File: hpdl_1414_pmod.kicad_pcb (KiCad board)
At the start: 2 copper layers, 84 x 56 mm, 6 parts, among them J1 10129382-912001BLF, J2 10129382-912001BLF

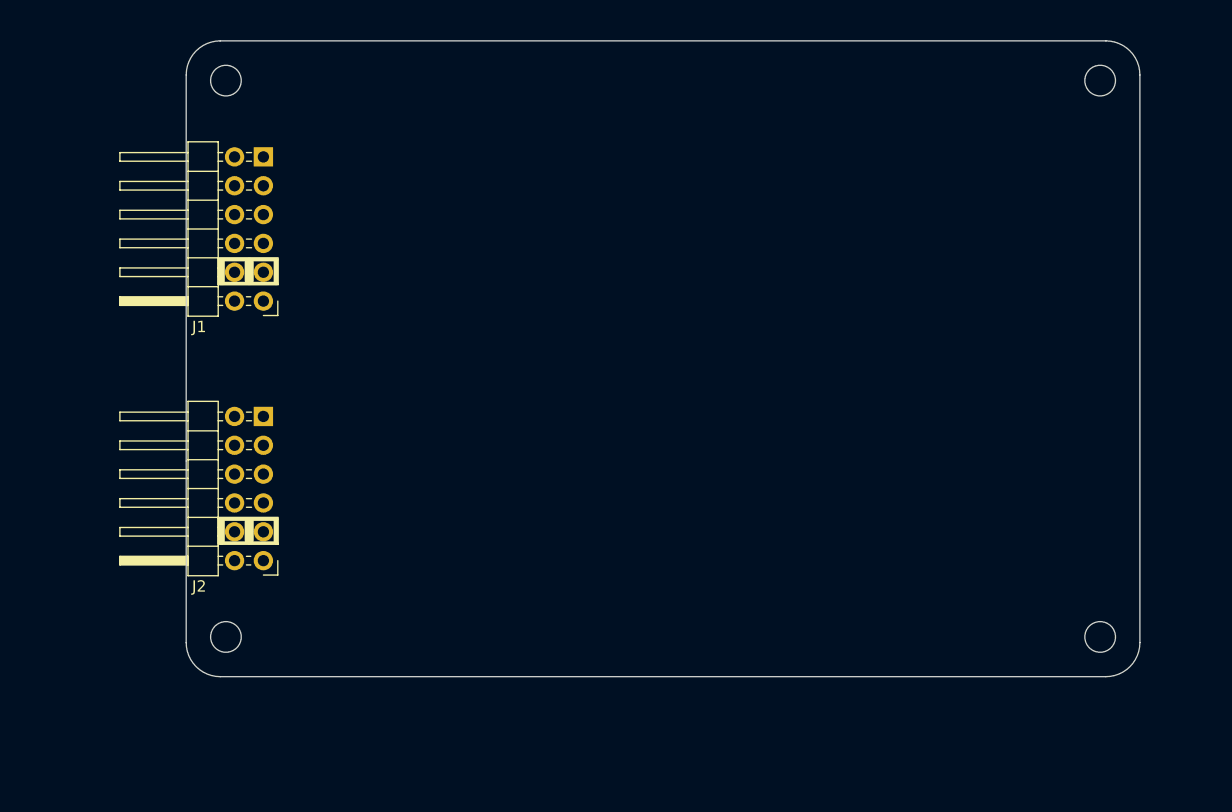
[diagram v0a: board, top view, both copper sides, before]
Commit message: Change pcb mounting hole type
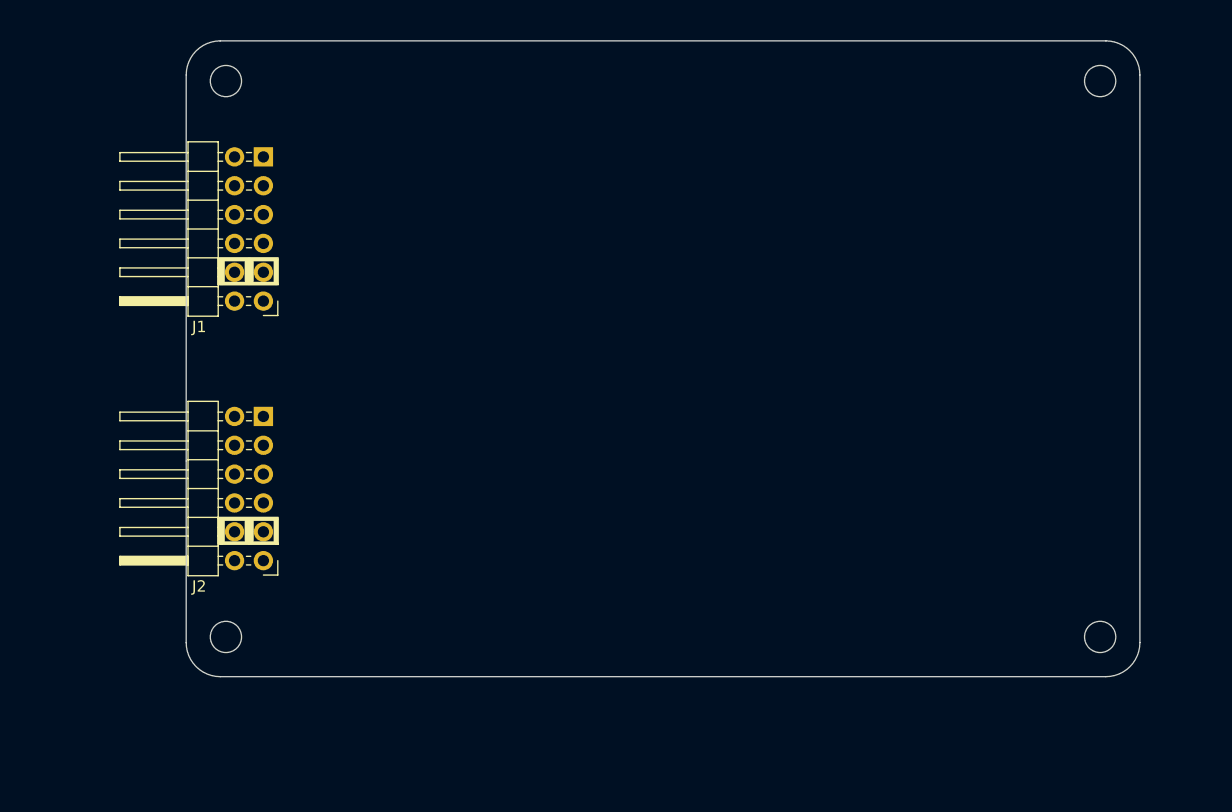
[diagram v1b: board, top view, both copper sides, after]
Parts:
- removed MH1, MH2, MH3, MH4: MountingHole_2.7mm_M2.5, MountingHole:MountingHole_2.7mm_M2.5
- added ?: , RPi_Hat:RPi_Hat_Mounting_Hole, F.Cu at (103.5, 96.5)
- added ?: , RPi_Hat:RPi_Hat_Mounting_Hole, F.Cu at (103.5, 47.5)
- added ?: , RPi_Hat:RPi_Hat_Mounting_Hole, F.Cu at (180.5, 47.5)
- added ?: , RPi_Hat:RPi_Hat_Mounting_Hole, F.Cu at (180.5, 96.5)
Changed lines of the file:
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@@
   (net 23 "unconnected-(J2-GND-Pad11)")
   (net 24 "unconnected-(J2-VCC-Pad12)")
-  (footprint "MountingHole:MountingHole_2.7mm_M2.5" locked (layer "F.Cu")
-    (at 180.5 47.5)
-    (descr "Mounting Hole 2.7mm, no annular, M2.5")
-    (tags "mounting hole 2.7mm no annular m2.5")
-    (attr board_only exclude_from_pos_files exclude_from_bom)
-    (fp_text reference "MH2" (at 0 4) (layer "F.Fab") hide
-        (effects (font (size 1 1) (thickness 0.15)))
-    )
-    (fp_text value "MountingHole_2.7mm_M2.5" (at 0 3.7) (layer "F.Fab") hide
-        (effects (font (size 1 1) (thickness 0.15)))
-    )
-    (fp_text user "${REFERENCE}" (at 0.3 0) (layer "F.Fab") hide
-        (effects (font (size 1 1) (thickness 0.15)))
-    )
-    (fp_circle (center 0 0) (end 2.7 0)
-      (stroke (width 0.15) (type solid)) (fill none) (layer "Cmts.User"))
-    (fp_circle (center 0 0) (end 2.95 0)
-      (stroke (width 0.05) (type solid)) (fill none) (layer "F.CrtYd"))
-    (pad "" np_thru_hole circle locked (at 0 0) (size 2.7 2.7) (drill 2.7) (layers "*.Cu" "*.Mask"))
-  )
-  (footprint "MountingHole:MountingHole_2.7mm_M2.5" locked (layer "F.Cu")
-    (at 103.5 96.5)
-    (descr "Mounting Hole 2.7mm, no annular, M2.5")
-    (tags "mounting hole 2.7mm no annular m2.5")
-    (attr board_only exclude_from_pos_files exclude_from_bom)
-    (fp_text reference "MH3" (at 0 -4) (layer "F.Fab") hide
-        (effects (font (size 1 1) (thickness 0.15)))
-    )
-    (fp_text value "MountingHole_2.7mm_M2.5" (at 0 3.7) (layer "F.Fab") hide
-        (effects (font (size 1 1) (thickness 0.15)))
-    )
-    (fp_text user "${REFERENCE}" (at 0.3 0) (layer "F.Fab") hide
-        (effects (font (size 1 1) (thickness 0.15)))
-    )
-    (fp_circle (center 0 0) (end 2.7 0)
-      (stroke (width 0.15) (type solid)) (fill none) (layer "Cmts.User"))
-    (fp_circle (center 0 0) (end 2.95 0)
-      (stroke (width 0.05) (type solid)) (fill none) (layer "F.CrtYd"))
-    (pad "" np_thru_hole circle locked (at 0 0) (size 2.7 2.7) (drill 2.7) (layers "*.Cu" "*.Mask"))
-  )
-  (footprint "MountingHole:MountingHole_2.7mm_M2.5" locked (layer "F.Cu")
-    (at 103.5 47.5)
-    (descr "Mounting Hole 2.7mm, no annular, M2.5")
-    (tags "mounting hole 2.7mm no annular m2.5")
-    (attr board_only exclude_from_pos_files exclude_from_bom)
-    (fp_text reference "MH1" (at 0 4) (layer "F.Fab") hide
-        (effects (font (size 1 1) (thickness 0.15)))
-    )
-    (fp_text value "MountingHole_2.7mm_M2.5" (at 0 3.7) (layer "F.Fab") hide
-        (effects (font (size 1 1) (thickness 0.15)))
-    )
-    (fp_text user "${REFERENCE}" (at 0.3 0) (layer "F.Fab") hide
-        (effects (font (size 1 1) (thickness 0.15)))
-    )
-    (fp_circle (center 0 0) (end 2.7 0)
-      (stroke (width 0.15) (type solid)) (fill none) (layer "Cmts.User"))
-    (fp_circle (center 0 0) (end 2.95 0)
-      (stroke (width 0.05) (type solid)) (fill none) (layer "F.CrtYd"))
-    (pad "" np_thru_hole circle locked (at 0 0) (size 2.7 2.7) (drill 2.7) (layers "*.Cu" "*.Mask"))
+  (footprint "RPi_Hat:RPi_Hat_Mounting_Hole" locked (layer "F.Cu")
+    (at 103.5 96.5 180)
+    (descr "Mounting hole, Befestigungsbohrung, 2,7mm, No Annular, Kein Restring,")
+    (tags "Mounting hole, Befestigungsbohrung, 2,7mm, No Annular, Kein Restring,")
+    (attr through_hole)
+    (fp_text reference "" (at 0 -4.0005 unlocked) (layer "F.SilkS") hide
+        (effects (font (size 1 1) (thickness 0.15)))
+    )
+    (fp_text value "" (at 0.09906 3.59918) (layer "F.Fab") hide
+        (effects (font (size 0.5 0.5) (thickness 0.07)))
+    )
+    (fp_circle (center 0 0) (end 3.1 0)
+      (stroke (width 0.15) (type solid)) (fill none) (layer "B.CrtYd"))
+    (fp_circle (center 0 0) (end 3.1 0)
+      (stroke (width 0.15) (type solid)) (fill none) (layer "F.CrtYd"))
+    (fp_circle (center 0 0) (end 1.375 0)
+      (stroke (width 0.15) (type solid)) (fill none) (layer "B.Fab"))
+    (fp_circle (center 0 0) (end 3.1 0)
+      (stroke (width 0.15) (type solid)) (fill none) (layer "B.Fab"))
+    (fp_circle (center 0 0) (end 1.375 0)
+      (stroke (width 0.15) (type solid)) (fill none) (layer "F.Fab"))
+    (fp_circle (center 0 0) (end 3.1 0)
+      (stroke (width 0.15) (type solid)) (fill none) (layer "F.Fab"))
+    (pad "" np_thru_hole circle locked (at 0 0 180) (size 2.75 2.75) (drill 2.75) (layers "F&B.Cu" "*.Mask")
+      (solder_mask_margin 1.725) (clearance 1.725))
+  )
+  (footprint "RPi_Hat:RPi_Hat_Mounting_Hole" locked (layer "F.Cu")
+    (at 103.5 47.54 180)
+    (descr "Mounting hole, Befestigungsbohrung, 2,7mm, No Annular, Kein Restring,")
+    (tags "Mounting hole, Befestigungsbohrung, 2,7mm, No Annular, Kein Restring,")
+    (attr through_hole)
+    (fp_text reference "" (at 0 -4.0005 unlocked) (layer "F.SilkS") hide
+        (effects (font (size 1 1) (thickness 0.15)))
+    )
+    (fp_text value "" (at 0.09906 3.59918) (layer "F.Fab") hide
+        (effects (font (size 0.5 0.5) (thickness 0.07)))
+    )
+    (fp_circle (center 0 0) (end 3.1 0)
+      (stroke (width 0.15) (type solid)) (fill none) (layer "B.CrtYd"))
+    (fp_circle (center 0 0) (end 3.1 0)
+      (stroke (width 0.15) (type solid)) (fill none) (layer "F.CrtYd"))
+    (fp_circle (center 0 0) (end 1.375 0)
+      (stroke (width 0.15) (type solid)) (fill none) (layer "B.Fab"))
+    (fp_circle (center 0 0) (end 3.1 0)
+      (stroke (width 0.15) (type solid)) (fill none) (layer "B.Fab"))
+    (fp_circle (center 0 0) (end 1.375 0)
+      (stroke (width 0.15) (type solid)) (fill none) (layer "F.Fab"))
+    (fp_circle (center 0 0) (end 3.1 0)
+      (stroke (width 0.15) (type solid)) (fill none) (layer "F.Fab"))
+    (pad "" np_thru_hole circle locked (at 0 0 180) (size 2.75 2.75) (drill 2.75) (layers "F&B.Cu" "*.Mask")
+      (solder_mask_margin 1.725) (clearance 1.725))
+  )
+  (footprint "RPi_Hat:RPi_Hat_Mounting_Hole" locked (layer "F.Cu")
+    (at 180.5 47.54 180)
+    (descr "Mounting hole, Befestigungsbohrung, 2,7mm, No Annular, Kein Restring,")
+    (tags "Mounting hole, Befestigungsbohrung, 2,7mm, No Annular, Kein Restring,")
+    (attr through_hole)
+    (fp_text reference "" (at 0 -4.0005 unlocked) (layer "F.SilkS") hide
+        (effects (font (size 1 1) (thickness 0.15)))
+    )
+    (fp_text value "" (at 0.09906 3.59918) (layer "F.Fab") hide
+        (effects (font (size 0.5 0.5) (thickness 0.07)))
+    )
+    (fp_circle (center 0 0) (end 3.1 0)
+      (stroke (width 0.15) (type solid)) (fill none) (layer "B.CrtYd"))
+    (fp_circle (center 0 0) (end 3.1 0)
+      (stroke (width 0.15) (type solid)) (fill none) (layer "F.CrtYd"))
+    (fp_circle (center 0 0) (end 1.375 0)
+      (stroke (width 0.15) (type solid)) (fill none) (layer "B.Fab"))
+    (fp_circle (center 0 0) (end 3.1 0)
+      (stroke (width 0.15) (type solid)) (fill none) (layer "B.Fab"))
+    (fp_circle (center 0 0) (end 1.375 0)
+      (stroke (width 0.15) (type solid)) (fill none) (layer "F.Fab"))
+    (fp_circle (center 0 0) (end 3.1 0)
+      (stroke (width 0.15) (type solid)) (fill none) (layer "F.Fab"))
+    (pad "" np_thru_hole circle locked (at 0 0 180) (size 2.75 2.75) (drill 2.75) (layers "F&B.Cu" "*.Mask")
+      (solder_mask_margin 1.725) (clearance 1.725))
   )
   (footprint "pmod:PinHeader_2x06_P2.54mm_PMODPeriph2B" locked (layer "F.Cu")
@@
     )
   )
-  (footprint "MountingHole:MountingHole_2.7mm_M2.5" locked (layer "F.Cu")
-    (at 180.5 96.5)
-    (descr "Mounting Hole 2.7mm, no annular, M2.5")
-    (tags "mounting hole 2.7mm no annular m2.5")
-    (attr board_only exclude_from_pos_files exclude_from_bom)
-    (fp_text reference "MH4" (at 0 -4) (layer "F.Fab") hide
-        (effects (font (size 1 1) (thickness 0.15)))
-    )
-    (fp_text value "MountingHole_2.7mm_M2.5" (at 0 3.7) (layer "F.Fab") hide
-        (effects (font (size 1 1) (thickness 0.15)))
-    )
-    (fp_text user "${REFERENCE}" (at 0.3 0) (layer "F.Fab") hide
-        (effects (font (size 1 1) (thickness 0.15)))
-    )
-    (fp_circle (center 0 0) (end 2.7 0)
-      (stroke (width 0.15) (type solid)) (fill none) (layer "Cmts.User"))
-    (fp_circle (center 0 0) (end 2.95 0)
-      (stroke (width 0.05) (type solid)) (fill none) (layer "F.CrtYd"))
-    (pad "" np_thru_hole circle locked (at 0 0) (size 2.7 2.7) (drill 2.7) (layers "*.Cu" "*.Mask"))
+  (footprint "RPi_Hat:RPi_Hat_Mounting_Hole" locked (layer "F.Cu")
+    (at 180.5 96.5 180)
+    (descr "Mounting hole, Befestigungsbohrung, 2,7mm, No Annular, Kein Restring,")
+    (tags "Mounting hole, Befestigungsbohrung, 2,7mm, No Annular, Kein Restring,")
+    (attr through_hole)
+    (fp_text reference "" (at 0 -4.0005 unlocked) (layer "F.SilkS") hide
+        (effects (font (size 1 1) (thickness 0.15)))
+    )
+    (fp_text value "" (at 0.09906 3.59918) (layer "F.Fab") hide
+        (effects (font (size 0.5 0.5) (thickness 0.07)))
+    )
+    (fp_circle (center 0 0) (end 3.1 0)
+      (stroke (width 0.15) (type solid)) (fill none) (layer "B.CrtYd"))
+    (fp_circle (center 0 0) (end 3.1 0)
+      (stroke (width 0.15) (type solid)) (fill none) (layer "F.CrtYd"))
+    (fp_circle (center 0 0) (end 1.375 0)
+      (stroke (width 0.15) (type solid)) (fill none) (layer "B.Fab"))
+    (fp_circle (center 0 0) (end 3.1 0)
+      (stroke (width 0.15) (type solid)) (fill none) (layer "B.Fab"))
+    (fp_circle (center 0 0) (end 1.375 0)
+      (stroke (width 0.15) (type solid)) (fill none) (layer "F.Fab"))
+    (fp_circle (center 0 0) (end 3.1 0)
+      (stroke (width 0.15) (type solid)) (fill none) (layer "F.Fab"))
+    (pad "" np_thru_hole circle locked (at 0 0 180) (size 2.75 2.75) (drill 2.75) (layers "F&B.Cu" "*.Mask")
+      (solder_mask_margin 1.725) (clearance 1.725))
   )
   (footprint "pmod:PinHeader_2x06_P2.54mm_PMODPeriph2B" locked (layer "F.Cu")

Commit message: Finilize shematic, place components, add 3d models
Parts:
- added C1: CP, Capacitor_THT:C_Disc_D4.3mm_W1.9mm_P5.00mm, F.Cu at (128.5, 85.5)
- added C2: CP, Capacitor_THT:C_Disc_D4.3mm_W1.9mm_P5.00mm, F.Cu at (146.5, 85.5)
- added C3: CP, Capacitor_THT:C_Disc_D4.3mm_W1.9mm_P5.00mm, F.Cu at (164.5, 85.5)
- added DS1: HPDL-1414, hpdl_1414:hpdl-1414, F.Cu at (119.5, 72.0)
- added DS2: HPDL-1414, hpdl_1414:hpdl-1414, F.Cu at (137.5, 72.0)
- added DS3: HPDL-1414, hpdl_1414:hpdl-1414, F.Cu at (155.5, 72.0)
- added DS4: HPDL-1414, hpdl_1414:hpdl-1414, F.Cu at (173.5, 72.0)
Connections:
- J1 pad 1: unconnected-(J1-IO1-Pad1) -> /D0
- J1 pad 11: unconnected-(J1-GND-Pad11) -> GND
- J1 pad 12: unconnected-(J1-VCC-Pad12) -> VDD
- J1 pad 2: unconnected-(J1-IO2-Pad2) -> /D1
- J1 pad 3: unconnected-(J1-IO3-Pad3) -> /D2
- J1 pad 4: unconnected-(J1-IO4-Pad4) -> /D3
- J1 pad 5: unconnected-(J1-GND-Pad5) -> GND
- J1 pad 6: unconnected-(J1-VCC-Pad6) -> VDD
- J1 pad 7: unconnected-(J1-IO5-Pad7) -> /D4
- J1 pad 8: unconnected-(J1-IO6-Pad8) -> /D5
- J1 pad 9: unconnected-(J1-IO7-Pad9) -> /D6
- J2 pad 1: unconnected-(J2-IO1-Pad1) -> /A0
- J2 pad 11: unconnected-(J2-GND-Pad11) -> GND
- J2 pad 12: unconnected-(J2-VCC-Pad12) -> VDD
- J2 pad 2: unconnected-(J2-IO2-Pad2) -> /A1
- J2 pad 3: unconnected-(J2-IO3-Pad3) -> /#WR1
- J2 pad 4: unconnected-(J2-IO4-Pad4) -> /#WR2
- J2 pad 5: unconnected-(J2-GND-Pad5) -> GND
- J2 pad 6: unconnected-(J2-VCC-Pad6) -> VDD
- J2 pad 7: unconnected-(J2-IO5-Pad7) -> /#WR3
- J2 pad 8: unconnected-(J2-IO6-Pad8) -> /#WR4

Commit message: Grenerate gerbers, V1.0
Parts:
- added C4: 15uF, Capacitor_SMD:C_1210_3225Metric_Pad1.33x2.70mm_HandSolder, F.Cu at (107.4, 72.1)
- added G***: LOGO, LOGO, F.Cu at (145.0, 52.0)
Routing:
- net VDD: track 0.00 -> 167.9 mm
- net /D4: track 0.00 -> 97.9 mm, vias 0 -> 4
- net /D5: track 0.00 -> 94.4 mm, vias 0 -> 4
- net /D6: track 0.00 -> 86.4 mm, vias 0 -> 4
- net /D0: track 0.00 -> 82.4 mm, vias 0 -> 4
- net /D1: track 0.00 -> 82.1 mm, vias 0 -> 4
- net /D2: track 0.00 -> 81.3 mm, vias 0 -> 4
- net /A1: track 0.00 -> 81.2 mm, vias 0 -> 4
- net /D3: track 0.00 -> 81.1 mm, vias 0 -> 4
- net /A0: track 0.00 -> 80.3 mm, vias 0 -> 4
- net /#WR4: track 0.00 -> 72.0 mm, vias 0 -> 1
- net /#WR3: track 0.00 -> 61.7 mm
- net /#WR2: track 0.00 -> 31.5 mm
- net /#WR1: track 0.00 -> 12.5 mm
- net GND: track 0.00 -> 11.7 mm
- added copper zone on B.Cu, net GND
